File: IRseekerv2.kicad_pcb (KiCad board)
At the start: 2 copper layers, 80 x 80 mm, 41 parts, among them J13 Conn_01x04_Pin, J14 Conn_01x02_Pin, J15 SEL_VOLTAGE, J16 G, J17 G, J18 G, J19 G, J20 Conn_01x02_Pin, J26 Conn_01x02_Pin, J27 Conn_01x02_Pin, J28 Conn_01x02_Pin, SW1 SW_Push, SW2 SW_Push, U10 TSSP4038, U11 TSSP4038, U12 TSSP4038, U13 TSSP4038, U14 TSSP4038, U15 TSSP4038, U16 TSSP4038, U17 AMS1117-3.3, U2 CD4012, U3 STM32G431CBUx, U4 CD4012B, U5 TSSP4038, U6 TSSP4038, U7 TSSP4038, U8 TSSP4038, U9 TSSP4038, Y1 Crystal

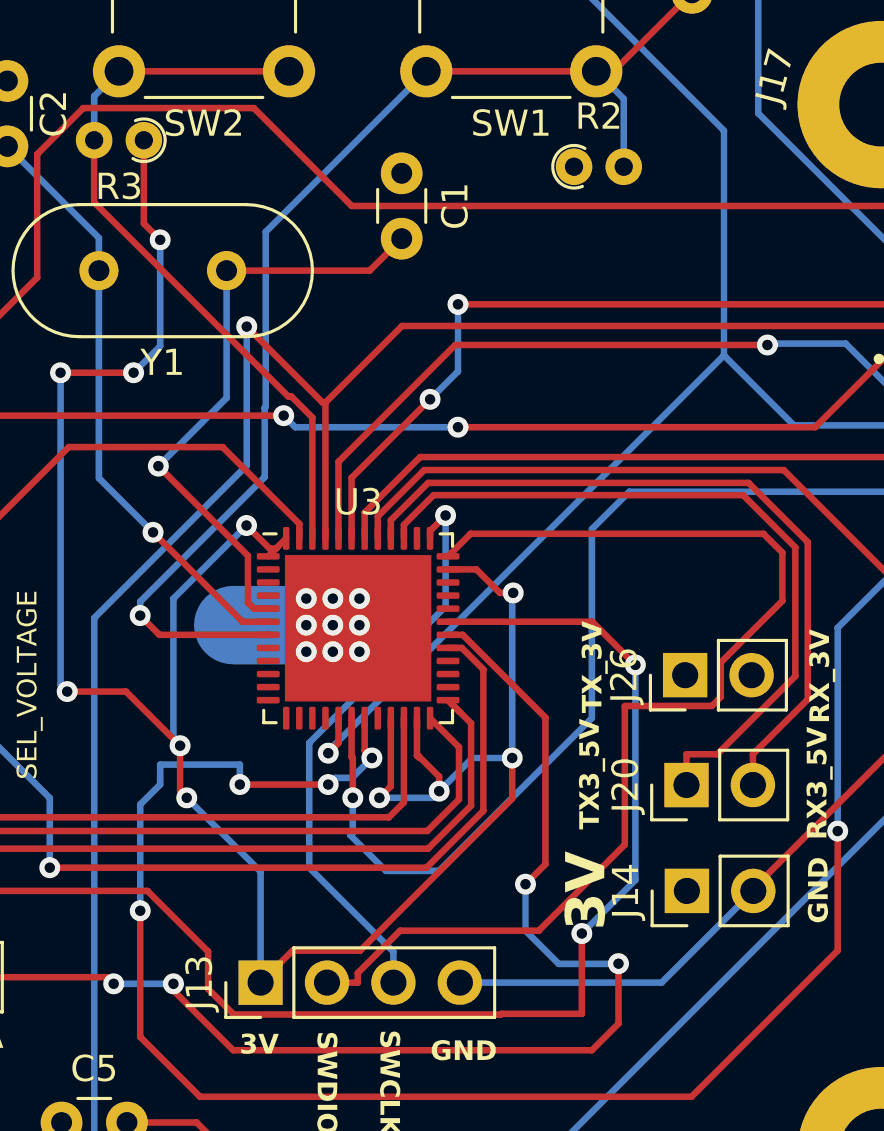
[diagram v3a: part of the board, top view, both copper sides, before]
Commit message: Disconnected mounting holes from ground, reroute some connections because of I2C pullups
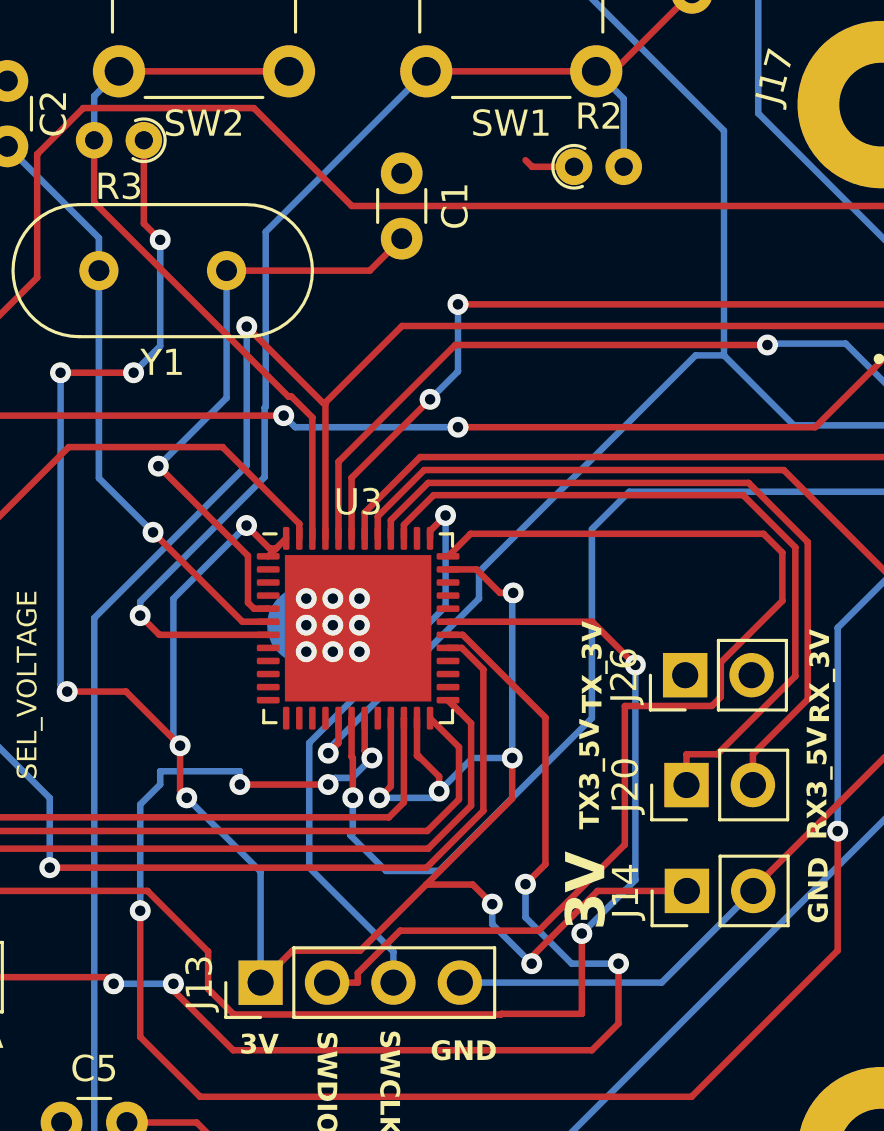
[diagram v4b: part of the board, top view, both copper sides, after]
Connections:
- J16 pad 1: GND -> unconnected-(J16-Pin_1-Pad1)
- J17 pad 1: GND -> unconnected-(J17-Pin_1-Pad1)
- J18 pad 1: GND -> unconnected-(J18-Pin_1-Pad1)
- J19 pad 1: GND -> unconnected-(J19-Pin_1-Pad1)
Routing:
- net +3.3V: track 91.9 -> 106.8 mm, vias 12 -> 14
- net GND: track 61.7 -> 58.9 mm
- net I1: track 63.9 -> 64.6 mm
- net I3: track 88.1 -> 87.6 mm

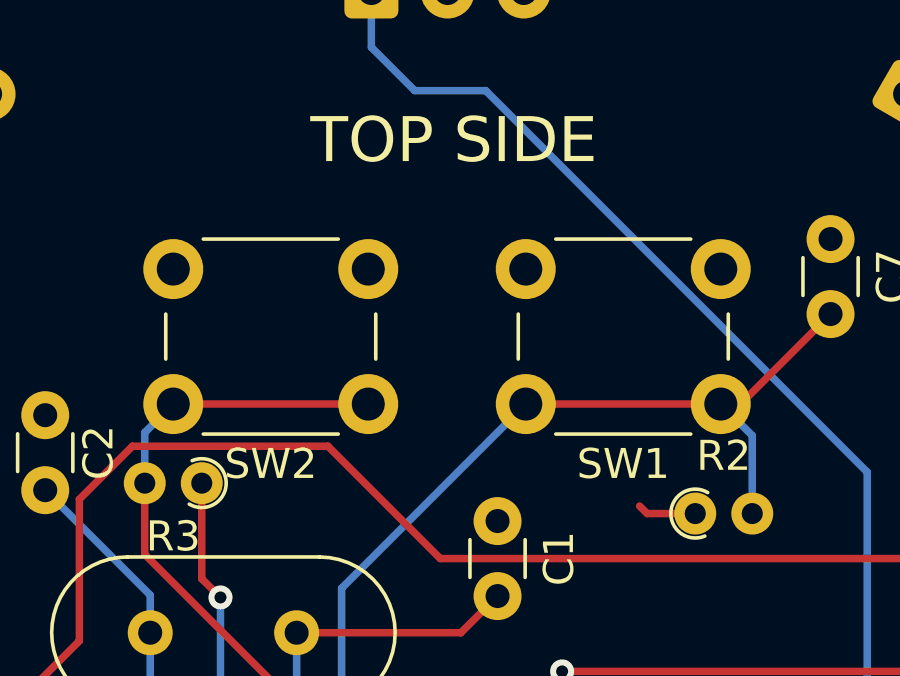
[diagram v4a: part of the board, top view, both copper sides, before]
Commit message: Added label to bottom side
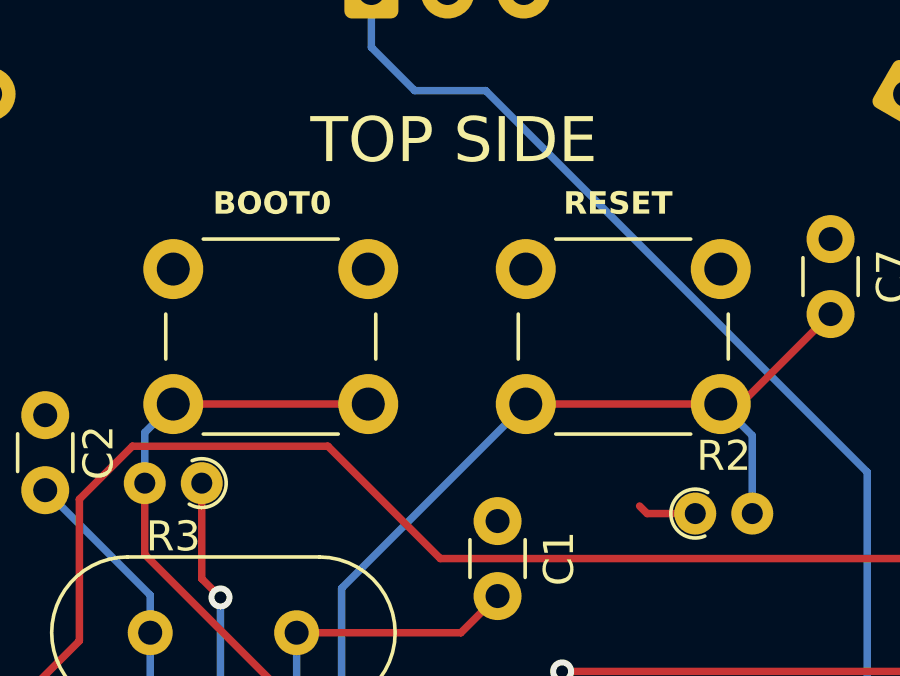
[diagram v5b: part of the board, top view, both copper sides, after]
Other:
- board text added: "BOOT0"
- board text added: "RESET"
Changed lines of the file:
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@@
     (property "ki_keywords" "switch normally-open pushbutton push-button")
     (attr through_hole)
-    (fp_text reference "SW2" (at 3.25 -2) (layer "F.SilkS")
+    (fp_text reference "SW2" (at 3.25 -2) (layer "F.SilkS") hide
         (effects (font (size 1 1) (thickness 0.15)))
     )
@@
     (property "ki_keywords" "switch normally-open pushbutton push-button")
     (attr through_hole)
-    (fp_text reference "SW1" (at 3.25 -2) (layer "F.SilkS")
+    (fp_text reference "SW1" (at 3.25 -2) (layer "F.SilkS") hide
         (effects (font (size 1 1) (thickness 0.15)))
     )
@@
   (gr_line (start 93.625 165.75) (end 93.375 21.75)
     (stroke (width 0.2) (type solid)) (layer "User.8"))
+  (gr_text "3V" (at 113.724 108.97 90) (layer "B.SilkS")
+    (effects (font (size 1.5 1.5) (thickness 0.3) bold) (justify left bottom mirror))
+  )
+  (gr_text "SDA" (at 90.424 116.586) (layer "B.SilkS")
+    (effects (font (size 0.75 0.75) (thickness 0.1875) bold) (justify left bottom mirror))
+  )
+  (gr_text "TX_3V" (at 113.474 100.73 90) (layer "B.SilkS")
+    (effects (font (size 0.75 0.75) (thickness 0.1875) bold) (justify left bottom mirror))
+  )
+  (gr_text "3V" (at 101.092 116.84) (layer "B.SilkS")
+    (effects (font (size 0.75 0.75) (thickness 0.1875) bold) (justify left bottom mirror))
+  )
+  (gr_text "SCL" (at 87.884 116.586) (layer "B.SilkS")
+    (effects (font (size 0.75 0.75) (thickness 0.1875) bold) (justify left bottom mirror))
+  )
+  (gr_text "SWDIO" (at 103.378 115.824 90) (layer "B.SilkS")
+    (effects (font (size 0.75 0.75) (thickness 0.1875) bold) (justify left bottom mirror))
+  )
+  (gr_text "GND" (at 122.174 109.22 90) (layer "B.SilkS")
+    (effects (font (size 0.75 0.75) (thickness 0.1875) bold) (justify left bottom mirror))
+  )
+  (gr_text "SWCLK" (at 105.918 115.824 -270) (layer "B.SilkS")
+    (effects (font (size 0.75 0.75) (thickness 0.1875) bold) (justify left bottom mirror))
+  )
+  (gr_text "TX3_5V" (at 113.474 104.286 90) (layer "B.SilkS")
+    (effects (font (size 0.75 0.75) (thickness 0.1875) bold) (justify left bottom mirror))
+  )
+  (gr_text "RX_3V" (at 122.174 100.33 90) (layer "B.SilkS")
+    (effects (font (size 0.75 0.75) (thickness 0.1875) bold) (justify left bottom mirror))
+  )
+  (gr_text "RX3_5V" (at 122.174 103.886 90) (layer "B.SilkS")
+    (effects (font (size 0.75 0.75) (thickness 0.1875) bold) (justify left bottom mirror))
+  )
+  (gr_text "GND" (at 109.22 117.094) (layer "B.SilkS")
+    (effects (font (size 0.75 0.75) (thickness 0.1875) bold) (justify left bottom mirror))
+  )
   (gr_text "RX_3V" (at 122.186 104.094 90) (layer "F.SilkS")
     (effects (font (size 0.75 0.75) (thickness 0.1875) bold) (justify left bottom))
@@
     (effects (font (size 0.75 0.75) (thickness 0.1875) bold) (justify left bottom))
   )
+  (gr_text "BOOT0" (at 96.266 72.898) (layer "F.SilkS")
+    (effects (font (size 0.75 0.75) (thickness 0.1875) bold) (justify left bottom))
+  )
   (gr_text "GND" (at 86.106 105.41) (layer "F.SilkS")
     (effects (font (size 1 1) (thickness 0.15)))
   )
+  (gr_text "RESET" (at 107.95 72.898) (layer "F.SilkS")
+    (effects (font (size 0.75 0.75) (thickness 0.1875) bold) (justify left bottom))
+  )
   (gr_text "RX3_5V" (at 122.086 108.544 90) (layer "F.SilkS")
